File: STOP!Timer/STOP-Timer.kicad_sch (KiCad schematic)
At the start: 27 parts, among them J1 Foot Switch Jack, J2 Conn_01x04_Pin, J3 XLR3, J4 Conn_01x04_Pin, Q2 AO3401A, SW1 SW_Push, SW2 SW_Push, SW3 SW_Push, SW4 SW_Push, SW5 SW_SPDT, SW6 SW_Push, SW7 SW_Push, SW8 SW_SPDT, U2 EC11E18244AU

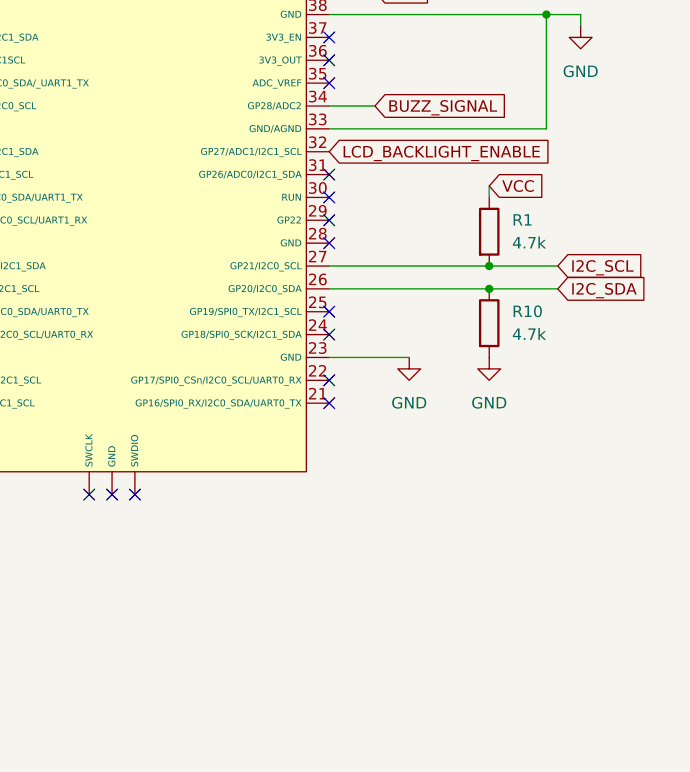
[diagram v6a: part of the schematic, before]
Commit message: Add flying Wire Display Connection Workaround
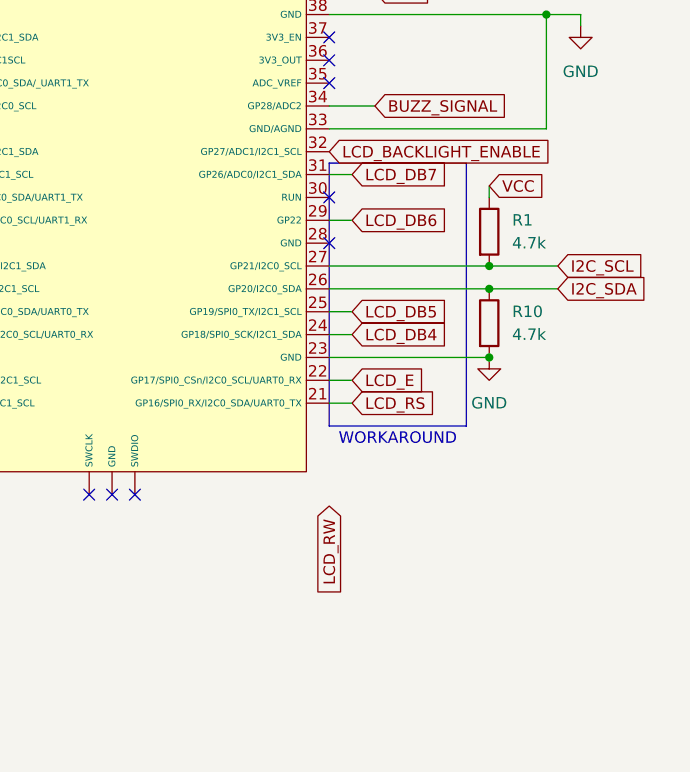
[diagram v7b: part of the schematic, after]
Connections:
- net LCD_RS: now reaches U1.21 (GP16/SPI0_RX/I2C0_SDA/UART0_TX)
- net LCD_E: now reaches U1.22 (GP17/SPI0_CSn/I2C0_SCL/UART0_RX)
- net LCD_DB4: now reaches U1.24 (GP18/SPI0_SCK/I2C1_SDA)
- net LCD_DB5: now reaches U1.25 (GP19/SPI0_TX/I2C1_SCL)
- net LCD_DB6: now reaches U1.29 (GP22)
- net LCD_DB7: now reaches U1.31 (GP26/ADC0/I2C1_SDA)
- no-connect marks 21 -> 15
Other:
- note added: "WORKAROUND"
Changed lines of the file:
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@@
 	(paper "A4")
 	(junction
+		(at 264.16 134.62)
+		(diameter 0)
+		(color 0 0 0 0)
+	)
+	(junction
 		(at 264.16 124.46)
 		(diameter 0)
@@
 	)
 	(no_connect
-		(at 246.38 132.08)
-	)
-	(no_connect
 		(at 246.38 99.06)
 	)
@@
 	)
 	(no_connect
-		(at 246.38 129.54)
-	)
-	(no_connect
 		(at 149.86 45.72)
 	)
@@
 	)
 	(no_connect
-		(at 246.38 139.7)
-	)
-	(no_connect
-		(at 246.38 137.16)
-	)
-	(no_connect
-		(at 246.38 119.38)
-	)
-	(no_connect
-		(at 246.38 114.3)
-	)
-	(no_connect
 		(at 198.12 93.98)
 	)
 	(wire
 		(pts
+			(xy 246.38 129.54) (xy 248.92 129.54)
+		)
+		(stroke
+			(width 0)
+			(type default)
+		)
+	)
+	(wire
+		(pts
 			(xy 250.19 30.48) (xy 250.19 34.29)
 		)
@@
 	(wire
 		(pts
+			(xy 246.38 119.38) (xy 248.92 119.38)
+		)
+		(stroke
+			(width 0)
+			(type default)
+		)
+	)
+	(wire
+		(pts
 			(xy 270.51 109.22) (xy 246.38 109.22)
 		)
@@
 	(wire
 		(pts
+			(xy 248.92 137.16) (xy 246.38 137.16)
+		)
+		(stroke
+			(width 0)
+			(type default)
+		)
+	)
+	(wire
+		(pts
 			(xy 55.88 91.44) (xy 60.96 91.44)
 		)
@@
 	(wire
 		(pts
+			(xy 246.38 114.3) (xy 248.92 114.3)
+		)
+		(stroke
+			(width 0)
+			(type default)
+		)
+	)
+	(wire
+		(pts
 			(xy 198.12 31.75) (xy 201.93 31.75)
 		)
@@
 	(wire
 		(pts
+			(xy 248.92 139.7) (xy 246.38 139.7)
+		)
+		(stroke
+			(width 0)
+			(type default)
+		)
+	)
+	(wire
+		(pts
 			(xy 134.62 33.02) (xy 134.62 21.59)
 		)
@@
 	(wire
 		(pts
+			(xy 246.38 132.08) (xy 248.92 132.08)
+		)
+		(stroke
+			(width 0)
+			(type default)
+		)
+	)
+	(wire
+		(pts
 			(xy 80.01 91.44) (xy 80.01 92.71)
 		)
@@
 	(wire
 		(pts
-			(xy 246.38 134.62) (xy 255.27 134.62)
+			(xy 246.38 134.62) (xy 264.16 134.62)
 		)
 		(stroke
@@
 	)
 	(rectangle
+		(start 246.38 113.03)
+		(end 261.62 142.24)
+		(stroke
+			(width 0)
+			(type default)
+			(color 255 0 24 1)
+		)
+		(fill
+			(type color)
+			(color 255 50 0 0.3)
+		)
+	)
+	(rectangle
 		(start 12.7 124.46)
 		(end 119.38 180.34)
@@
 		)
 	)
+	(text "WORKAROUND\n"
+		(exclude_from_sim no)
+		(at 254 143.764 0)
+		(effects
+			(font
+				(size 1.27 1.27)
+				(color 255 34 28 1)
+			)
+		)
+	)
 	(text "SPECIAL MODE SELECTION SWITCHES"
 		(exclude_from_sim no)
@@
 		)
 	)
+	(global_label "LCD_RW"
+		(shape input)
+		(at 246.38 151.13 270)
+		(fields_autoplaced yes)
+		(effects
+			(font
+				(size 1.27 1.27)
+			)
+			(justify right)
+		)
+		(property "Intersheetrefs" "${INTERSHEET_REFS}"
+			(at 246.38 161.3723 90)
+			(effects
+				(font
+					(size 1.27 1.27)
+				)
+				(justify right)
+				(hide yes)
+			)
+		)
+	)
 	(global_label "ENCODER_SEL"
 		(shape input)
@@
 		)
 	)
+	(global_label "LCD_RS"
+		(shape input)
+		(at 248.92 139.7 0)
+		(fields_autoplaced yes)
+		(effects
+			(font
+				(size 1.27 1.27)
+			)
+			(justify left)
+		)
+		(property "Intersheetrefs" "${INTERSHEET_REFS}"
+			(at 258.9204 139.7 0)
+			(effects
+				(font
+					(size 1.27 1.27)
+				)
+				(justify left)
+				(hide yes)
+			)
+		)
+	)
 	(global_label "VCC"
 		(shape input)
@@
 		)
 	)
+	(global_label "LCD_DB7"
+		(shape input)
+		(at 248.92 114.3 0)
+		(fields_autoplaced yes)
+		(effects
+			(font
+				(size 1.27 1.27)
+			)
+			(justify left)
+		)
+		(property "Intersheetrefs" "${INTERSHEET_REFS}"
+			(at 260.1904 114.3 0)
+			(effects
+				(font
+					(size 1.27 1.27)
+				)
+				(justify left)
+				(hide yes)
+			)
+		)
+	)
 	(global_label "ENCODER_B"
 		(shape input)
@@
 		)
 	)
+	(global_label "LCD_DB4"
+		(shape input)
+		(at 248.92 132.08 0)
+		(fields_autoplaced yes)
+		(effects
+			(font
+				(size 1.27 1.27)
+			)
+			(justify left)
+		)
+		(property "Intersheetrefs" "${INTERSHEET_REFS}"
+			(at 260.1904 132.08 0)
+			(effects
+				(font
+					(size 1.27 1.27)
+				)
+				(justify left)
+				(hide yes)
+			)
+		)
+	)
 	(global_label "ENCODER_SEL"
 		(shape input)
@@
 		)
 	)
+	(global_label "LCD_DB5"
+		(shape input)
+		(at 248.92 129.54 0)
+		(fields_autoplaced yes)
+		(effects
+			(font
+				(size 1.27 1.27)
+			)
+			(justify left)
+		)
+		(property "Intersheetrefs" "${INTERSHEET_REFS}"
+			(at 260.1904 129.54 0)
+			(effects
+				(font
+					(size 1.27 1.27)
+				)
+				(justify left)
+				(hide yes)
+			)
+		)
+	)
 	(global_label "TIME_SEL_2"
 		(shape input)
@@
 		)
 	)
+	(global_label "LCD_DB6"
+		(shape input)
+		(at 248.92 119.38 0)
+		(fields_autoplaced yes)
+		(effects
+			(font
+				(size 1.27 1.27)
+			)
+			(justify left)
+		)
+		(property "Intersheetrefs" "${INTERSHEET_REFS}"
+			(at 260.1904 119.38 0)
+			(effects
+				(font
+					(size 1.27 1.27)
+				)
+				(justify left)
+				(hide yes)
+			)
+		)
+	)
 	(global_label "INDICATOR_TIME_2"
 		(shape input)
@@
 		)
 	)
+	(global_label "LCD_E"
+		(shape input)
+		(at 248.92 137.16 0)
+		(fields_autoplaced yes)
+		(effects
+			(font
+				(size 1.27 1.27)
+			)
+			(justify left)
+		)
+		(property "Intersheetrefs" "${INTERSHEET_REFS}"
+			(at 257.5899 137.16 0)
+			(effects
+				(font
+					(size 1.27 1.27)
+				)
+				(justify left)
+				(hide yes)
+			)
+		)
+	)
 	(symbol
 		(lib_id "power:GND")
@@
 					(unit 1)
 				)
-			)
-		)
-	)
-	(symbol
-		(lib_id "power:GND")
-		(at 255.27 134.62 0)
-		(unit 1)
-		(exclude_from_sim no)
-		(in_bom yes)
-		(on_board yes)
-		(dnp no)
-		(fields_autoplaced yes)
-		(property "Reference" "#PWR02"
-			(at 255.27 140.97 0)
-			(effects
-				(font
-					(size 1.27 1.27)
-				)
-				(hide yes)
-			)
-		)
-		(property "Value" "GND"
-			(at 255.27 139.7 0)
-			(effects
-				(font
-					(size 1.27 1.27)
-				)
-			)
-		)
-		(property "Footprint" ""
-			(at 255.27 134.62 0)
-			(effects
-				(font
-					(size 1.27 1.27)
-				)
-				(hide yes)
-			)
-		)
-		(property "Datasheet" ""
-			(at 255.27 134.62 0)
-			(effects
-				(font
-					(size 1.27 1.27)
-				)
-				(hide yes)
-			)
-		)
-		(property "Description" "Power symbol creates a global label with name \"GND\" , ground"
-			(at 255.27 134.62 0)
-			(effects
-				(font
-					(size 1.27 1.27)
-				)
-				(hide yes)
-			)
-		)
-		(pin "1"
-		)
-		(instances
-			(project "STOP-Timer"
-				(path "/f7118eea-cf2d-4aa4-9e6e-b7551058ec7f"
-					(reference "#PWR02")
-					(unit 1)
-				)

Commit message: Update
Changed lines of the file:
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@@
 (kicad_sch
-	(version 20231120)
+	(version 20250114)
 	(generator "eeschema")
-	(generator_version "8.0")
+	(generator_version "9.0")
 	(paper "A4")
+	(rectangle
+		(start 12.7 68.58)
+		(end 106.68 124.46)
+		(stroke
+			(width 0)
+			(type default)
+		)
+		(fill
+			(type none)
+		)
+	)
+	(rectangle
+		(start 246.38 113.03)
+		(end 261.62 142.24)
+		(stroke
+			(width 0)
+			(type default)
+			(color 255 0 24 1)
+		)
+		(fill
+			(type color)
+			(color 255 50 0 0.3)
+		)
+	)
+	(rectangle
+		(start 12.7 124.46)
+		(end 119.38 180.34)
+		(stroke
+			(width 0)
+			(type default)
+		)
+		(fill
+			(type none)
+		)
+	)
+	(rectangle
+		(start 12.7 12.7)
+		(end 60.96 68.58)
+		(stroke
+			(width 0)
+			(type default)
+		)
+		(fill
+			(type none)
+		)
+	)
+	(rectangle
+		(start 60.96 12.7)
+		(end 106.68 68.58)
+		(stroke
+			(width 0)
+			(type default)
+		)
+		(fill
+			(type none)
+		)
+	)
+	(rectangle
+		(start 119.38 124.46)
+		(end 157.48 180.34)
+		(stroke
+			(width 0)
+			(type default)
+		)
+		(fill
+			(type none)
+		)
+	)
+	(rectangle
+		(start 233.68 12.7)
+		(end 284.48 68.58)
+		(stroke
+			(width 0)
+			(type default)
+		)
+		(fill
+			(type none)
+		)
+	)
+	(rectangle
+		(start 106.68 12.7)
+		(end 154.94 83.82)
+		(stroke
+			(width 0)
+			(type default)
+		)
+		(fill
+			(type none)
+		)
+	)
+	(text "MENU ENCODER"
+		(exclude_from_sim no)
+		(at 131.572 15.24 0)
+		(effects
+			(font
+				(face "Roboto")
+				(size 1.27 1.27)
+			)
+		)
+	)
+	(text "SELECTED TIME INDICATOR\n"
+		(exclude_from_sim no)
+		(at 83.82 15.24 0)
+		(effects
+			(font
+				(face "Roboto")
+				(size 1.27 1.27)
+			)
+		)
+	)
+	(text "TIME SELECTOR BUTTONS"
+		(exclude_from_sim no)
+		(at 55.372 73.66 0)
+		(effects
+			(font
+				(face "Roboto")
+				(size 1.27 1.27)
+			)
+		)
+	)
+	(text "Switch Signal Out\n"
+		(exclude_from_sim no)
+		(at 260.35 15.748 0)
+		(effects
+			(font
+				(face "Roboto")
+				(size 1.27 1.27)
+			)
+		)
+	)
+	(text "WORKAROUND\n"
+		(exclude_from_sim no)
+		(at 254 143.764 0)
+		(effects
+			(font
+				(size 1.27 1.27)
+				(color 255 34 28 1)
+			)
+		)
+	)
+	(text "SPECIAL MODE SELECTION SWITCHES"
+		(exclude_from_sim no)
+		(at 55.372 129.794 0)
+		(effects
+			(font
+				(face "Roboto")
+				(size 1.27 1.27)
+			)
+		)
+	)
+	(text "CONNECTOR TO FRONT PANEL BOARD"
+		(exclude_from_sim no)
+		(at 139.446 128.27 0)
+		(effects
+			(font
+				(face "Roboto")
+				(size 1.27 1.27)
+			)
+		)
+	)
+	(text "Foot Start Switch\n"
+		(exclude_from_sim no)
+		(at 34.544 15.494 0)
+		(effects
+			(font
+				(face "Roboto")
+				(size 1.27 1.27)
+			)
+		)
+	)
+	(text "Focus Switch\n"
+		(exclude_from_sim no)
+		(at 32.766 144.78 0)
+		(effects
+			(font
+				(size 1.27 1.27)
+			)
+		)
+	)
 	(junction
 		(at 264.16 134.62)
@@
 		)
 	)
-	(rectangle
-		(start 12.7 68.58)
-		(end 106.68 124.46)
-		(stroke
-			(width 0)
-			(type default)
-		)
-		(fill
-			(type none)
-		)
-	)
-	(rectangle
-		(start 246.38 113.03)
-		(end 261.62 142.24)
-		(stroke
-			(width 0)
-			(type default)
-			(color 255 0 24 1)
-		)
-		(fill
-			(type color)
-			(color 255 50 0 0.3)
-		)
-	)
-	(rectangle
-		(start 12.7 124.46)
-		(end 119.38 180.34)
-		(stroke
-			(width 0)
-			(type default)
-		)
-		(fill
-			(type none)
-		)
-	)
-	(rectangle
-		(start 12.7 12.7)
-		(end 60.96 68.58)
-		(stroke
-			(width 0)
-			(type default)
-		)
-		(fill
-			(type none)
-		)
-	)
-	(rectangle
-		(start 60.96 12.7)
-		(end 106.68 68.58)
-		(stroke
-			(width 0)
-			(type default)
-		)
-		(fill
-			(type none)
-		)
-	)
-	(rectangle
-		(start 119.38 124.46)
-		(end 157.48 180.34)
-		(stroke
-			(width 0)
-			(type default)
-		)
-		(fill
-			(type none)
-		)
-	)
-	(rectangle
-		(start 233.68 12.7)
-		(end 284.48 68.58)
-		(stroke
-			(width 0)
-			(type default)
-		)
-		(fill
-			(type none)
-		)
-	)
-	(rectangle
-		(start 106.68 12.7)
-		(end 154.94 83.82)
-		(stroke
-			(width 0)
-			(type default)
-		)
-		(fill
-			(type none)
-		)
-	)
-	(text "MENU ENCODER"
-		(exclude_from_sim no)
-		(at 131.572 15.24 0)
-		(effects
-			(font
-				(face "Roboto")
-				(size 1.27 1.27)
-			)
-		)
-	)
-	(text "SELECTED TIME INDICATOR\n"
-		(exclude_from_sim no)
-		(at 83.82 15.24 0)
-		(effects
-			(font
-				(face "Roboto")
-				(size 1.27 1.27)
-			)
-		)
-	)
-	(text "TIME SELECTOR BUTTONS"
-		(exclude_from_sim no)
-		(at 55.372 73.66 0)
-		(effects
-			(font
-				(face "Roboto")
-				(size 1.27 1.27)
-			)
-		)
-	)
-	(text "Switch Signal Out\n"
-		(exclude_from_sim no)
-		(at 260.35 15.748 0)
-		(effects
-			(font
-				(face "Roboto")
-				(size 1.27 1.27)
-			)
-		)
-	)
-	(text "WORKAROUND\n"
-		(exclude_from_sim no)
-		(at 254 143.764 0)
-		(effects
-			(font
-				(size 1.27 1.27)
-				(color 255 34 28 1)
-			)
-		)
-	)
-	(text "SPECIAL MODE SELECTION SWITCHES"
-		(exclude_from_sim no)
-		(at 55.372 129.794 0)
-		(effects
-			(font
-				(face "Roboto")
-				(size 1.27 1.27)
-			)
-		)
-	)
-	(text "CONNECTOR TO FRONT PANEL BOARD"
-		(exclude_from_sim no)
-		(at 139.446 128.27 0)
-		(effects
-			(font
-				(face "Roboto")
-				(size 1.27 1.27)
-			)
-		)
-	)
-	(text "Foot Start Switch\n"
-		(exclude_from_sim no)
-		(at 34.544 15.494 0)
-		(effects
-			(font
-				(face "Roboto")
-				(size 1.27 1.27)
-			)
-		)
-	)
-	(text "Focus Switch\n"
-		(exclude_from_sim no)
-		(at 32.766 144.78 0)
-		(effects
-			(font
-				(size 1.27 1.27)
-			)
-		)
-	)
 	(global_label "TIME_SEL_3"
 		(shape input)
@@
 		(at 153.67 -27.94)
 		(size 27.94 17.78)
+		(exclude_from_sim no)
+		(in_bom yes)
+		(on_board yes)
+		(dnp no)
 		(fields_autoplaced yes)
 		(stroke
@@
 		)
 	)
+	(embedded_fonts no)
 )
